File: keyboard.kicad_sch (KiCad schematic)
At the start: 74 parts, among them J1 USB_C_Receptacle_USB2.0_14P, Q1 NMOS, SW1 SW_Push, SW10 SW_Push, SW11 RotaryEncoder_Switch, SW2 SW_Push, SW3 SW_Push, SW4 SW_Push, SW5 SW_Push, SW6 SW_Push, SW7 SW_Push, SW8 SW_Push, SW9 SW_Push, U1 STM32F072CBT6, U2 USBLC6-2P6, U4 LDO40LPU33RY

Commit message: Added footprints and placement
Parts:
- removed C15: 4.7u, symbol Device:C
- removed C9: 1u, symbol Device:C
- removed FB1: 120R, symbol Device:FerriteBead
- removed J1: USB_C_Receptacle_USB2.0_14P, symbol Connector:USB_C_Receptacle_USB2.0_14P
- removed R24, R25: 330R, symbol Device:R
- added C13: 4.7u, Capacitor_SMD:C_0805_2012Metric, symbol Device:C
- added J1: USB_C_Receptacle_USB2.0_16P, my_footprints:UJ20CHGMSMT4BP16TR, symbol Connector:USB_C_Receptacle_USB2.0_16P
- added J3: Conn_01x10_Pin, Connector_PinHeader_1.00mm:PinHeader_2x05_P1.00mm_Vertical, symbol Connector:Conn_01x10_Pin
- added R15, R18: 330R, Resistor_SMD:R_0402_1005Metric, symbol Device:R
- added U3, U5: SN74LV1T34DBV, Package_TO_SOT_SMD:SOT-23-5, symbol Logic_LevelTranslator:SN74LV1T34DBV
- C1, C10, C11, C12, C2, C3, C5: footprint (none) -> Capacitor_SMD:C_0402_1005Metric; Mouser Part Number (none) -> 81-GRM022C81A104ME5L; Mouser Price/Stock (none) -> https://www.mouser.pl/ProductDetail/YAGEO/RC0402JR-7D330RL?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
- C14, C4, C6: footprint (none) -> Capacitor_SMD:C_0805_2012Metric; Mouser Part Number (none) -> 81-GRM21R61A475KE34D; Mouser Price/Stock (none) -> https://www.mouser.pl/ProductDetail/Murata-Electronics/GRM2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
- C7: value 10n -> 100n; footprint (none) -> Capacitor_SMD:C_0402_1005Metric; Mouser Part Number (none) -> 81-GRM022C81A104ME5L; Mouser Price/Stock (none) -> https://www.mouser.pl/ProductDetail/YAGEO/RC0402JR-7D330RL?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
- C8: footprint (none) -> Capacitor_SMD:C_0402_1005Metric; Mouser Part Number (none) -> 81-GXT155R61A105KE1D; Mouser Price/Stock (none) -> https://www.mouser.pl/ProductDetail/Murata-Electronics/GXT1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
- D10, D11, D12, D13, D14, D15, D16, D17, D18: footprint (none) -> LED_THT:LED_D3.0mm; Mouser Part Number (none) -> 630-HLMP-Y301-F0000; Mouser Price/Stock (none) -> https://www.mouser.pl/ProductDetail/Broadcom-Avago/HLMP-Y30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
- DS2: footprint NHD0208BZFLYBW -> NHD:NHD0208BZFLYBW
- Q1: footprint (none) -> my_footprints:SOT95P230X110-3N; Mouser Part Number (none) -> 771-NX3020NAK-QR
- R1, R11, R12, R13, R14: footprint (none) -> Resistor_SMD:R_0402_1005Metric; Mouser Part Number (none) -> 755-ESR01MZPJ103; Mouser Price/Stock (none) -> https://www.mouser.pl/ProductDetail/ROHM-Semiconductor/ESR0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
- R10: footprint (none) -> Resistor_SMD:R_0402_1005Metric; Mouser Part Number (none) -> 603-RC0402JR-7D330RL; Mouser Price/Stock (none) -> https://www.mouser.pl/ProductDetail/YAGEO/RC0402JR-7D330RL?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
- R16, R17: footprint (none) -> Resistor_SMD:R_0402_1005Metric; Mouser Part Number  (none) -> 71-RCC04025K10FKED
- R19, R2, R20, R21, R22, R23, R3, R4, R5, R6, R7, R8, R9: footprint (none) -> Resistor_SMD:R_0402_1005Metric; Mouser Part Number (none) -> 603-RC0402JR-7D330RL
- RV1: footprint (none) -> my_footprints:601030; Manufacturer_Part_Number (none) -> 581-601030
- SW1: footprint (none) -> my_footprints:TS0266100BK100LCRD; Mouser Part Number (none) -> 179-TS026655BK260LCR
- SW11: footprint (none) -> my_footprints:PEC12R3220FS0024; Mouser Part Number (none) -> 652-PEC12R3220FS0024
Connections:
- net +3.3VA is gone; now on net +3.3V: C7.1, C8.1, U1.9 (VDDA)
- net +3.3V: now also J3.7 (Pin_7), J3.8 (Pin_8); no longer R11.1, R12.2
- net +3V3: now also C14.1, U3.5 (VCC), U5.5 (VCC)
- net +5V: now also R11.1, R12.2, C13.1, J1.A4 (VBUS), J1.A9 (VBUS), J1.B4 (VBUS), J1.B9 (VBUS), R15.1, R18.1; no longer C14.1
- net GND: now also C11.2, C12.1, R1.2, C13.2, J1.A1 (GND), J1.A12 (GND), J1.B1 (GND), J1.B12 (GND), J1.S1 (SHIELD), J3.5 (Pin_5), J3.6 (Pin_6), U3.3 (GND), U5.3 (GND); no longer C11.1, C12.2, R1.1
- net LED+: now also R15.2, R18.2
- net NRST: now also J3.1 (Pin_1)
- net OUT_A: now also U5.4 (Y); no longer C11.2, R13.1
- net OUT_B: now also U3.4 (Y); no longer C12.1, R14.1
- net SWCLK: now also J3.2 (Pin_2)
- net SWDIO: now also J3.4 (Pin_4)
- net at R11.2, SW11.A: now also R14.2; no longer R13.2
- net at R12.1, SW11.B: now also R13.2; no longer R14.2
- net at R17.1: now also J1.A5 (CC1)
- net at SW1.2, U1.44 (BOOT0): now also R1.1; no longer R1.2
- net at R16.1: now also J1.B5 (CC2)
- net at U2.1 (I/O1): now also J1.A7 (D-), J1.B7 (D-)
- net at U2.3 (I/O2): now also J1.A6 (D+), J1.B6 (D+)
- new net: C12.2, R14.1, U5.2 (A)
- new net: C11.1, R13.1, U3.2 (A)
- no-connect marks 4 -> 26
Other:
- moved on the sheet: R11, SW11

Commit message: Added pcb routing
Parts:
- removed U2: USBLC6-2P6, Package_TO_SOT_SMD:SOT-666, symbol Power_Protection:USBLC6-2P6
- added U6: USBLC6-2SC6, Package_TO_SOT_SMD:SOT-23-6, symbol Power_Protection:USBLC6-2SC6
- J1: footprint my_footprints:UJ20CHGMSMT4BP16TR -> Connector_USB:USB_C_Receptacle_GCT_USB4105-xx-A_16P_TopMnt_Horizontal; Mouser Part Number 179-CHGMSMT4BP16TR -> 640-USB4105-GF-A
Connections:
- net +3V3 is gone; now on net +3.3V: C14.1, U3.5 (VCC), U4.4 (Vout), U4.5 (Vsense), U5.5 (VCC)
- net +5V: now also U6.5 (VBUS)
- net Column 1: now also U1.2 (PC13); no longer U1.17 (PA7)
- net Column 2: now also U1.3 (PC14); no longer U1.16 (PA6)
- net Column 3: now also U1.4 (PC15); no longer U1.15 (PA5)
- net DB4: now also U1.25 (PB12); no longer U1.22 (PB11)
- net DB5: now also U1.26 (PB13); no longer U1.25 (PB12)
- net DB6: now also U1.27 (PB14); no longer U1.26 (PB13)
- net DB7: now also U1.28 (PB15); no longer U1.27 (PB14)
- net GND: now also U6.2 (GND)
- net LCD_ENABLE: now also U1.12 (PA2); no longer U1.21 (PB10)
- net LCD_RS: now also U1.11 (PA1); no longer U1.46 (PB9)
- net MUTE: now also U1.39 (PB3); no longer U1.43 (PB7)
- net OUT_A: now also U1.41 (PB5); no longer U1.40 (PB4)
- net OUT_B: now also U1.40 (PB4); no longer U1.41 (PB5)
- net Row 1: now also U1.13 (PA3); no longer U1.31 (PA10)
- net Row 2: now also U1.14 (PA4); no longer U1.30 (PA9)
- net Row 3: now also U1.15 (PA5); no longer U1.29 (PA8)
- net SWCLK: now also J3.4 (Pin_4); no longer J3.2 (Pin_2)
- net SWDIO: now also J3.2 (Pin_2); no longer J3.4 (Pin_4)
- net USB_D+: now also U6.4 (I/O2)
- net USB_D-: now also U6.6 (I/O1)
- net at J1.A6 (D+), J1.B6 (D+): now also U6.3 (I/O2)
- net at J1.A7 (D-), J1.B7 (D-): now also U6.1 (I/O1)
- no-connect marks 26 -> 27

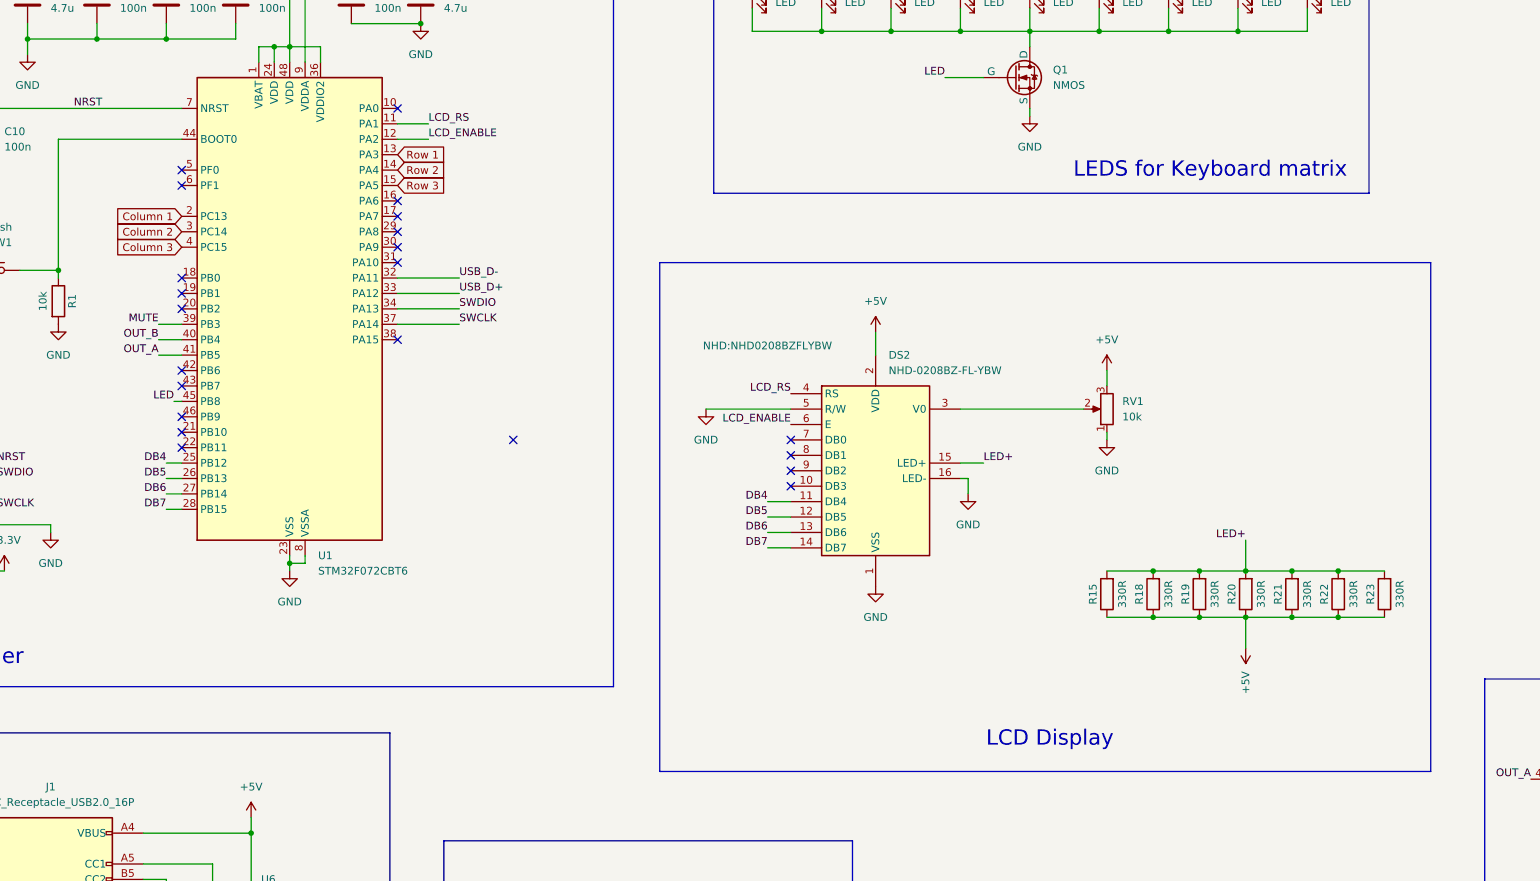
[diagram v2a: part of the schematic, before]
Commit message: Added oled footprint
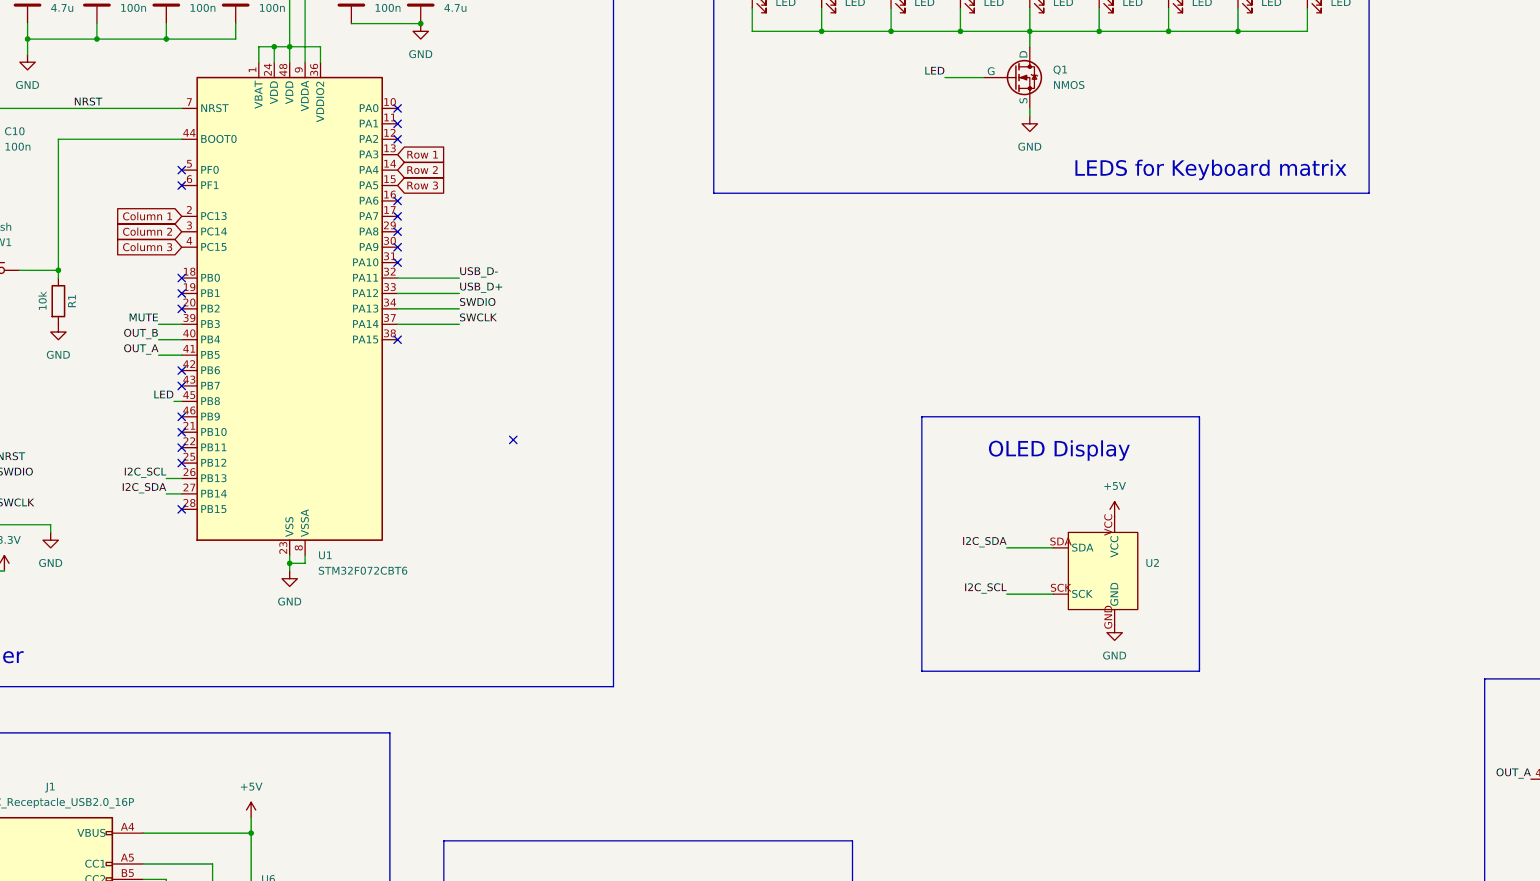
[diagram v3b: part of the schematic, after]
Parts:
- removed DS2: NHD-0208BZ-FL-YBW, NHD:NHD0208BZFLYBW, symbol NHD-0208BZ-FL-YBW:NHD-0208BZ-FL-YBW
- removed R15, R18, R19, R20, R21, R22, R23: 330R, Resistor_SMD:R_0402_1005Metric, symbol Device:R
- removed RV1: 10k, my_footprints:601030, symbol Device:R_Potentiometer
- added U2: ~, oled:Bez_nazwy, symbol oled:SH1106_OLED
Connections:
- net +5V: now also U2.VCC
- net GND: now also U2.GND
- net DB4: no longer names the net of U1.25 (PB12)
- net DB5 renamed I2C_SCL
- net I2C_SCL: now also U2.SCK
- net DB6 renamed I2C_SDA
- net I2C_SDA: now also U2.SDA
- net DB7: no longer names the net of U1.28 (PB15)
- net LCD_ENABLE: no longer names the net of U1.12 (PA2)
- net LCD_RS: no longer names the net of U1.11 (PA1)
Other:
- note added: "OLED Display"
- note removed: "LCD Display"
